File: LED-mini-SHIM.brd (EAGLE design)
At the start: 50.8 x 12.7 mm, 26 parts, among them IC1 TXB0101DCKR

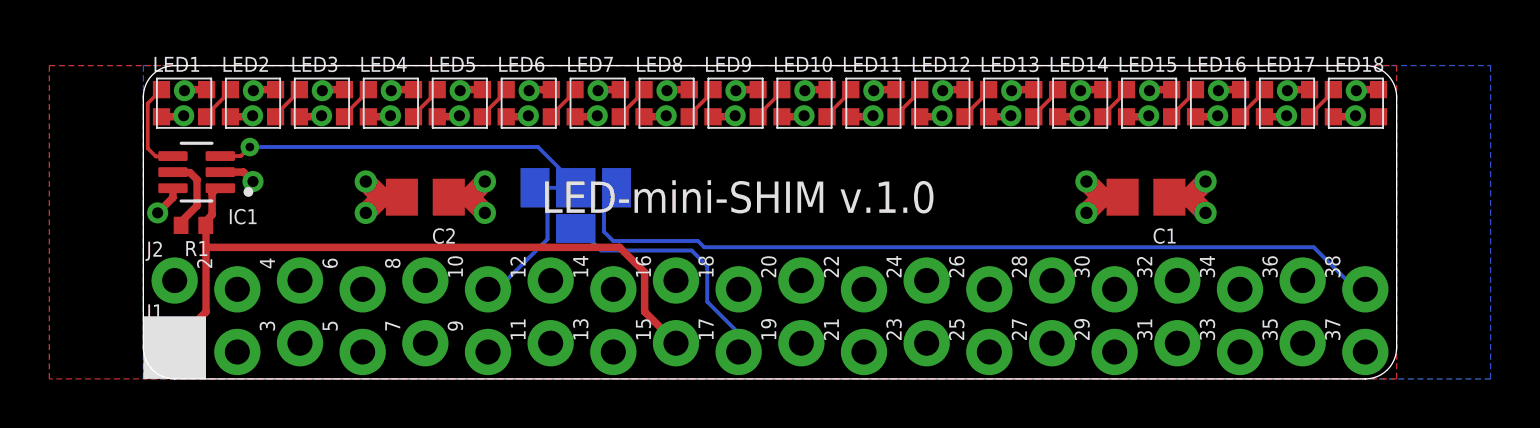
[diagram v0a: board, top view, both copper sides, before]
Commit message: Moved some traces and vias around
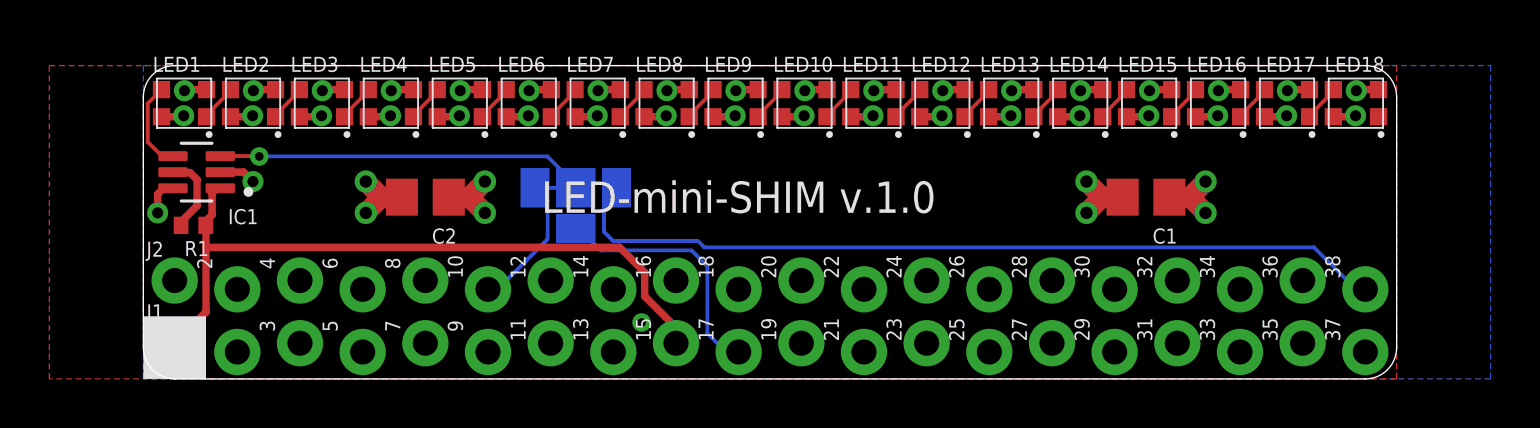
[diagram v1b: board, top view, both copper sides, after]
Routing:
- net 5V: track 23.0 -> 23.2 mm, vias 23 -> 24
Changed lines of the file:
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@@
 <drawing>
 <settings>
-<setting alwaysvectorfont="yes"/>
+<setting alwaysvectorfont="no"/>
 <setting verticaltext="up"/>
 </settings>
@@
 <wire x1="2.992" y1="7.732" x2="3.119" y2="7.732" width="0.3048" layer="1"/>
 <wire x1="2.992" y1="7.732" x2="2.786" y2="7.526" width="0.3048" layer="1"/>
-<wire x1="21.59" y1="1.4478" x2="20.32" y2="2.7178" width="0.3048" layer="1"/>
-<wire x1="20.32" y1="2.7178" x2="20.32" y2="4.318" width="0.3048" layer="1"/>
+<wire x1="21.59" y1="1.4478" x2="21.59" y2="2.0828" width="0.3048" layer="1"/>
+<wire x1="21.59" y1="2.0828" x2="20.32" y2="3.3528" width="0.3048" layer="1"/>
+<wire x1="20.32" y1="3.3528" x2="20.32" y2="4.318" width="0.3048" layer="1"/>
 <wire x1="20.32" y1="4.318" x2="19.304" y2="5.334" width="0.3048" layer="1"/>
 <wire x1="19.304" y1="5.334" x2="2.54" y2="5.334" width="0.3048" layer="1"/>
@@
 <contactref element="C1" pad="2"/>
 <contactref element="C2" pad="2"/>
-<polygon width="0.1524" layer="16" isolate="0.254">
+<polygon width="0.1524" layer="16" isolate="0.254" thermals="no">
 <vertex x="0" y="0"/>
 <vertex x="0" y="12.7"/>
@@
 <vertex x="54.61" y="0"/>
 </polygon>
-<polygon width="0.1524" layer="2" isolate="0.254">
+<polygon width="0.1524" layer="2" isolate="0.254" thermals="no">
 <vertex x="0" y="0"/>
 <vertex x="0" y="16.51"/>
@@
 <contactref element="J1" pad="10"/>
 <contactref element="SJ1" pad="4"/>
-<wire x1="24.13" y1="1.0922" x2="24.13" y2="1.8542" width="0.1524" layer="16"/>
-<wire x1="24.13" y1="1.8542" x2="22.86" y2="3.1242" width="0.1524" layer="16"/>
-<wire x1="22.86" y1="3.1242" x2="22.86" y2="4.572" width="0.1524" layer="16"/>
+<wire x1="24.13" y1="1.0922" x2="23.622" y2="1.0922" width="0.1524" layer="16"/>
+<wire x1="23.622" y1="1.0922" x2="22.86" y2="1.8542" width="0.1524" layer="16"/>
+<wire x1="22.86" y1="1.8542" x2="22.86" y2="4.572" width="0.1524" layer="16"/>
 <wire x1="22.86" y1="4.572" x2="22.225" y2="5.207" width="0.1524" layer="16"/>
 <wire x1="18.542" y1="5.207" x2="17.653" y2="6.096" width="0.1524" layer="16"/>
@@
 <contactref element="J2" pad="6"/>
 <contactref element="SJ1" pad="3"/>
+<wire x1="13.97" y1="3.6322" x2="14.351" y2="3.6322" width="0.1524" layer="16"/>
 <wire x1="16.383" y1="5.6642" x2="14.351" y2="3.6322" width="0.1524" layer="16"/>
-<wire x1="13.97" y1="3.6322" x2="14.351" y2="3.6322" width="0.1524" layer="16"/>
 <wire x1="15.875" y1="7.747" x2="16.383" y2="7.239" width="0.1524" layer="16"/>
 <wire x1="16.383" y1="7.239" x2="16.383" y2="5.6642" width="0.1524" layer="16"/>
@@
 <contactref element="C1" pad="1"/>
 <contactref element="C2" pad="1"/>
-<polygon width="0.1524" layer="1" isolate="0.254">
+<polygon width="0.1524" layer="1" isolate="0.254" thermals="no">
 <vertex x="-3.81" y="0"/>
 <vertex x="-3.81" y="12.7"/>
@@
 <vertex x="50.8" y="0"/>
 </polygon>
-<polygon width="0.1524" layer="15" isolate="0.254">
+<polygon width="0.1524" layer="15" isolate="0.254" thermals="no">
 <vertex x="0" y="-3.81"/>
 <vertex x="0" y="12.7"/>
@@
 <wire x1="49.0914" y1="10.626" x2="49.1334" y2="10.668" width="0.3048" layer="1"/>
 <via x="49.1334" y="10.668" extent="1-16" drill="0.45"/>
-<wire x1="1.199" y1="7.732" x2="1.199" y2="7.3494" width="0.3048" layer="1"/>
-<wire x1="1.199" y1="7.3494" x2="0.5806" y2="6.731" width="0.3048" layer="1"/>
+<wire x1="0.8196" y1="7.732" x2="0.5806" y2="7.493" width="0.3048" layer="1"/>
+<wire x1="0.5806" y1="7.493" x2="0.5806" y2="6.731" width="0.3048" layer="1"/>
+<wire x1="1.199" y1="7.732" x2="0.8196" y2="7.732" width="0.3048" layer="1"/>
 <via x="0.5806" y="6.731" extent="1-16" drill="0.45"/>
 <wire x1="13.208" y1="7.366" x2="13.843" y2="6.731" width="0.8128" layer="1"/>
@@
 <wire x1="42.418" y1="7.366" x2="43.053" y2="8.001" width="0.8128" layer="1"/>
 <via x="43.053" y="8.001" extent="1-16" drill="0.5"/>
+<via x="20.193" y="2.286" extent="1-16" drill="0.35"/>
 </signal>
 <signal name="N$1">
@@
 <wire x1="0.736" y1="11.726" x2="0.736" y2="11.7254875" width="0.1524" layer="1"/>
 <wire x1="0.736" y1="11.7254875" x2="0.1778" y2="11.1672875" width="0.1524" layer="1"/>
-<wire x1="0.1778" y1="11.1672875" x2="0.1778" y2="9.3472" width="0.1524" layer="1"/>
-<wire x1="0.1778" y1="9.3472" x2="0.508" y2="9.017" width="0.1524" layer="1"/>
-<wire x1="0.508" y1="9.017" x2="1.184" y2="9.017" width="0.1524" layer="1"/>
+<wire x1="0.1778" y1="11.1672875" x2="0.1778" y2="9.6012" width="0.1524" layer="1"/>
+<wire x1="0.1778" y1="9.6012" x2="0.762" y2="9.017" width="0.1524" layer="1"/>
+<wire x1="0.762" y1="9.017" x2="1.184" y2="9.017" width="0.1524" layer="1"/>
 <wire x1="1.184" y1="9.017" x2="1.199" y2="9.032" width="0.1524" layer="1"/>
 </signal>
@@
 <contactref element="IC1" pad="3"/>
 <contactref element="SJ1" pad="2"/>
-<wire x1="3.119" y1="9.032" x2="3.952" y2="9.032" width="0.1524" layer="1"/>
-<wire x1="3.952" y1="9.032" x2="4.318" y2="9.398" width="0.1524" layer="1"/>
-<via x="4.318" y="9.398" extent="1-16" drill="0.35"/>
-<wire x1="4.318" y1="9.398" x2="16.002" y2="9.398" width="0.1524" layer="16"/>
+<wire x1="3.119" y1="9.032" x2="4.684" y2="9.032" width="0.1524" layer="1"/>
+<wire x1="4.684" y1="9.032" x2="4.699" y2="9.017" width="0.1524" layer="1"/>
+<via x="4.699" y="9.017" extent="1-16" drill="0.35"/>
+<wire x1="4.699" y1="9.017" x2="16.383" y2="9.017" width="0.1524" layer="16"/>
 <wire x1="17.526" y1="7.874" x2="17.526" y2="7.747" width="0.1524" layer="16"/>
-<wire x1="16.002" y1="9.398" x2="17.526" y2="7.874" width="0.1524" layer="16"/>
+<wire x1="16.383" y1="9.017" x2="17.526" y2="7.874" width="0.1524" layer="16"/>
 </signal>
 <signal name="N$143">
